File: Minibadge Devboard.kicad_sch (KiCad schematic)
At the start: 37 parts, among them SW1 Power, U1 DRV8837C, U2 74HC4060

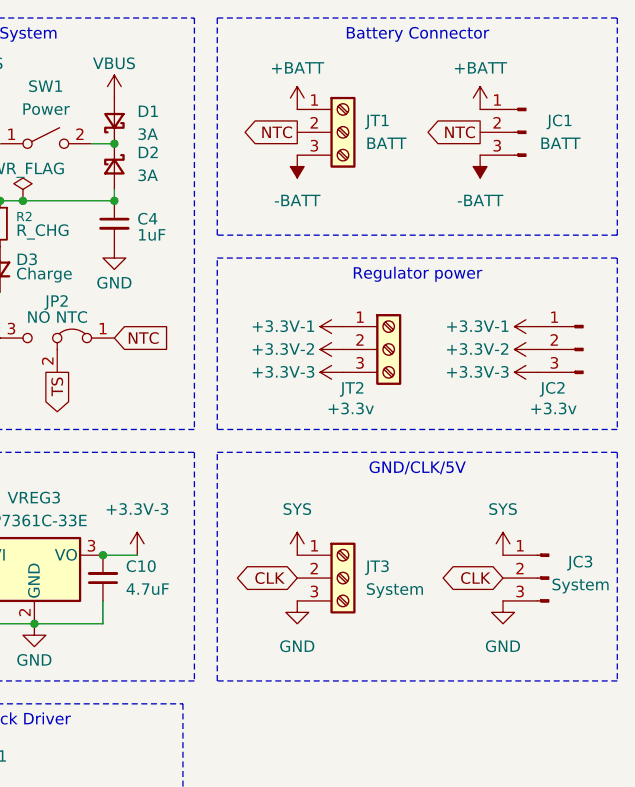
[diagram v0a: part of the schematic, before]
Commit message: Add WAGO 2059 for smaller footprint
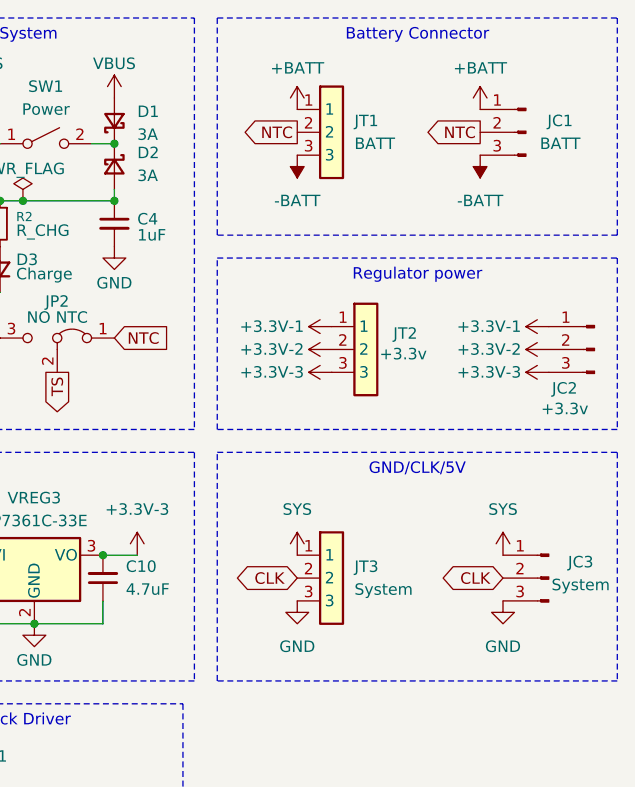
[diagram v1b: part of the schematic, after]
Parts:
- JT1, JT2, JT3: symbol Connector:Screw_Terminal_01x03 -> WAGO 2060:WAGO 2060-3pin; Arrow Part Number (none) -> 2060-453/998-404; Arrow Price/Stock (none) -> https://www.arrow.com/en/products/2060-453998-404/wago-kont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; Height (none) -> 4.5; Manufacturer_Name (none) -> Wago; Manufacturer_Part_Number (none) -> 2060-453/998-404
- U2: footprint 74LV4060D,118:74LV4060D118 -> (none)
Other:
- moved on the sheet: JC2

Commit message: update footprints
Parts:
- JC1, JC2, JC3: footprint Connector_PinSocket_2.54mm:PinSocket_1x03_P2.54mm_Vertical -> Castellated pins:Castellated pins 1x03
- JT1, JT2, JT3: footprint WAGO connectors:WAGO 2060-453 -> WAGO 2059-303:2059-303
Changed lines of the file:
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@@
 			)
 		)
-		(property "Footprint" "WAGO connectors:WAGO 2060-453"
+		(property "Footprint" "WAGO 2059-303:2059-303"
 			(at 200.66 144.45 0)
 			(effects
@@
 			)
 		)
-		(property "Footprint" "Connector_PinSocket_2.54mm:PinSocket_1x03_P2.54mm_Vertical"
+		(property "Footprint" "Castellated pins:Castellated pins 1x03"
 			(at 207.01 52.07 0)
 			(effects
@@
 			)
 		)
-		(property "Footprint" "WAGO connectors:WAGO 2060-453"
+		(property "Footprint" "WAGO 2059-303:2059-303"
 			(at 204.47 168.58 0)
 			(effects
@@
 			)
 		)
-		(property "Footprint" "WAGO connectors:WAGO 2060-453"
+		(property "Footprint" "WAGO 2059-303:2059-303"
 			(at 200.66 193.98 0)
 			(effects
@@
 			)
 		)
-		(property "Footprint" "Connector_PinSocket_2.54mm:PinSocket_1x03_P2.54mm_Vertical"
+		(property "Footprint" "Castellated pins:Castellated pins 1x03"
 			(at 209.55 101.6 0)
 			(effects
@@
 			)
 		)
-		(property "Footprint" "Connector_PinSocket_2.54mm:PinSocket_1x03_P2.54mm_Vertical"
+		(property "Footprint" "Castellated pins:Castellated pins 1x03"
 			(at 214.63 76.2 0)
 			(effects

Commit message: R1
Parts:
- removed JP1: Speed, symbol Jumper:Jumper_3_Bridged12
- removed JP2: NO NTC, symbol Jumper:Jumper_3_Bridged12
- added Q1: PMOS, Package_TO_SOT_SMD:SOT-23, symbol Simulation_SPICE:PMOS
- added R8: 100k, Resistor_SMD:R_0603_1608Metric, symbol Device:R_Small
- added SW3: SPEED, Jumper:SolderJumper-3_P1.3mm_Open_RoundedPad1.0x1.5mm_NumberLabels, symbol Switch:SW_SPDT
- added SW4: NTC, Jumper:SolderJumper-3_P1.3mm_Open_RoundedPad1.0x1.5mm_NumberLabels, symbol Switch:SW_SPDT
- JC1, JC2, JC3: now left out of the parts list
- JT1, JT2, JT3: LCSC Part # (none) -> C3309252
- NT1: footprint (none) -> NetTie:NetTie-2_SMD_Pad2.0mm
- SW1: footprint (none) -> SK12D07VG3-T:SW-SMD_SK12D07VG3-T; LCSC Part # (none) -> C25168821
- U1: LCSC Part # (none) -> C191000
- U2: footprint (none) -> Package_SO:TSSOP-16-1EP_4.4x5mm_P0.65mm; LCSC Part # (none) -> C354054
- USB1: footprint (none) -> Connector_USB:USB_C_Receptacle_HRO_TYPE-C-31-M-17
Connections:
- net +BATT: now also JC1.3 (Pin_3), JT1.3; no longer JC1.1 (Pin_1), JT1.1
- net -BATT: now also JC1.1 (Pin_1), JT1.1; no longer JC1.3 (Pin_3), JT1.3
- net CLK_LOW: now also SW3.2 (B)
- net FAST: now also SW3.1 (A)
- net GND: now also R8.2
- net NTC: now also SW4.3 (C)
- net SLOW: now also SW3.3 (C)
- net SYS: now also Q1.1 (D); no longer SW1.1 (A)
- net TS: now also SW4.2 (B)
- net VDD: now reaches D1.1 (K), D2.1 (K)
- net VDD: now also Q1.3 (S); no longer SW1.2 (B)
- net at R7.1: now also SW4.1 (A)
- new net: Q1.2 (G), SW1.1 (A)
- new net: R8.1, SW1.2 (B)
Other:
- moved on the sheet: BMS1, C1, C10, C2, C3, C4, C5, C6, C7, C8, C9, D1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

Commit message: Add support for external PSU and Power switch
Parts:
- added J1: External power, Castellated pins:Castellated pins 1x02, symbol Connector:Conn_01x02_Pin
- added J2: External switch, Castellated pins:Castellated pins 1x02, symbol Connector:Conn_01x02_Pin
- D3: value Charge -> RED
- R1: value 8.45k -> 8.45kΩ
- R3: value 20k -> 20kΩ
- R4, R5: value 5.1k -> 5.1kΩ
- R6: value 675 -> 675Ω
- R7: value 10k -> 10kΩ
- R8: value 100k -> 100kΩ
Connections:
- net GND: now also J1.1 (Pin_1)
- net VBUS: now also J1.2 (Pin_2)
- net SW1: now reaches Q1.2 (G), SW1.1 (A)
- net SW1: now also J2.1 (Pin_1)
- net SW2: now reaches R8.1, SW1.2 (B)
- net SW2: now also J2.2 (Pin_2)
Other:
- moved on the sheet: BMS1, C1, C10, C2, C3, C4, C5, C6, C7, C8, C9, D1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

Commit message: BOM updates
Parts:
- D1, D2: LCSC Part # (none) -> C382787
- D3: footprint LED_SMD:LED_1206_3216Metric -> LED_SMD:LED_0603_1608Metric; LCSC Part # (none) -> C2286
- J1, J2: now not fitted; now left out of the parts list
- JC1, JC2, JC3: now not fitted
- Q1: LCSC Part # (none) -> C347478
- USB1: LCSC Part # C3743528 -> C283540
- VREG1, VREG2, VREG3: LCSC Part # C3743528 -> C3743528
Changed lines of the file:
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@@
 		(unit 1)
 		(exclude_from_sim no)
-		(in_bom yes)
+		(in_bom no)
 		(on_board yes)
-		(dnp no)
+		(dnp yes)
 		(property "Reference" "J2"
 			(at 146.05 148.082 90)
@@
 			)
 		)
-		(property "Footprint" "LED_SMD:LED_1206_3216Metric"
+		(property "Footprint" "LED_SMD:LED_0603_1608Metric"
 			(at 134.62 52.07 90)
 			(effects
@@
 			)
 		)
+		(property "LCSC Part #" "C2286"
+			(at 134.62 52.07 90)
+			(effects
+				(font
+					(size 1.27 1.27)
+				)
+				(hide yes)
+			)
+		)
 		(pin "2"
 		)
@@
 			)
 		)
-		(property "LCSC Part #" "C3743528 "
+		(property "LCSC Part #" "C3743528"
 			(at 74.93 82.55 0)
 			(effects
@@
 		(in_bom no)
 		(on_board yes)
-		(dnp no)
+		(dnp yes)
 		(property "Reference" "JC1"
 			(at 196.85 36.83 0)
@@
 		(unit 1)
 		(exclude_from_sim no)
-		(in_bom yes)
+		(in_bom no)
 		(on_board yes)
-		(dnp no)
+		(dnp yes)
 		(property "Reference" "J1"
 			(at 129.286 148.082 90)
@@
 			)
 		)
+		(property "LCSC Part #" "C382787"
+			(at 147.32 40.64 90)
+			(effects
+				(font
+					(size 1.27 1.27)
+				)
+				(hide yes)
+			)
+		)
 		(pin "2"
 		)
@@
 			)
 		)
+		(property "LCSC Part #" "C347478"
+			(at 171.45 111.76 0)
+			(effects
+				(font
+					(size 1.27 1.27)
+				)
+				(hide yes)
+			)
+		)
 		(pin "2"
 		)
@@
 			)
 		)
-		(property "LCSC Part #" "C3743528 "
+		(property "LCSC Part #" "C3743528"
 			(at 138.43 82.55 0)
 			(effects
@@
 		(in_bom no)
 		(on_board yes)
-		(dnp no)
+		(dnp yes)
 		(property "Reference" "JC3"
 			(at 199.136 83.312 0)
@@
 			)
 		)
-		(property "LCSC Part #" "C3743528 "
+		(property "LCSC Part #" "C3743528"
 			(at 106.68 82.55 0)
 			(effects
@@
 			)
 		)
-		(property "LCSC Part #" "C3743528 "
+		(property "LCSC Part #" "C283540"
 			(at 71.12 43.18 0)
 			(effects
@@
 			)
 		)
+		(property "LCSC Part #" "C382787"
+			(at 147.32 35.56 90)
+			(effects
+				(font
+					(size 1.27 1.27)
+				)
+				(hide yes)
+			)
+		)
 		(pin "2"
 		)
@@
 		(in_bom no)
 		(on_board yes)
-		(dnp no)
+		(dnp yes)
 		(property "Reference" "JC2"
 			(at 197.358 64.008 0)

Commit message: LCSC part numbers
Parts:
- C1, C2: LCSC Part # (none) -> C14663
- C10, C5, C6, C7, C8, C9: LCSC Part # (none) -> C1779
- C3, C4: LCSC Part # (none) -> C15849
- R1: LCSC Part # (none) -> C25981
- R2: value R_CHG -> R_CHG 120-150Ω
- R3: LCSC Part # (none) -> C4184
- R4, R5: LCSC Part # (none) -> C23186
- R6: LCSC Part # (none) -> C23228
- R7: LCSC Part # (none) -> C25804
- R8: LCSC Part # (none) -> C25803
- SW3, SW4: now left out of the parts list
- VREG1, VREG2, VREG3: LCSC Part # C3743528 -> C500795
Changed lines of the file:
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@@
 			)
 		)
-		(property "LCSC Part #" "C3743528"
+		(property "LCSC Part #" "C500795"
 			(at 74.93 82.55 0)
 			(effects
@@
 			)
 		)
+		(property "LCSC Part #" "C1779"
+			(at 114.3 85.09 0)
+			(effects
+				(font
+					(size 1.27 1.27)
+				)
+				(hide yes)
+			)
+		)
 		(pin "2"
 		)
@@
 			)
 		)
+		(property "LCSC Part #" "C14663"
+			(at 64.77 111.76 90)
+			(effects
+				(font
+					(size 1.27 1.27)
+				)
+				(hide yes)
+			)
+		)
 		(pin "1"
 		)
@@
 			)
 		)
-		(property "Value" "R_CHG"
+		(property "Value" "R_CHG 120-150Ω"
 			(at 136.398 47.752 0)
 			(effects
@@
 			)
 		)
+		(property "LCSC Part #" ""
+			(at 134.62 46.99 0)
+			(effects
+				(font
+					(size 1.27 1.27)
+				)
+				(hide yes)
+			)
+		)
 		(pin "2"
 		)
@@
 			)
 		)
+		(property "LCSC Part #" "C23228"
+			(at 107.95 57.15 0)
+			(effects
+				(font
+					(size 1.27 1.27)
+				)
+				(hide yes)
+			)
+		)
 		(pin "2"
 		)
@@
 			)
 		)
-		(property "LCSC Part #" "C3743528"
+		(property "LCSC Part #" "C500795"
 			(at 138.43 82.55 0)
 			(effects
@@
 			)
 		)
+		(property "LCSC Part #" "C14663"
+			(at 88.9 109.22 90)
+			(effects
+				(font
+					(size 1.27 1.27)
+				)
+				(hide yes)
+			)
+		)
 		(pin "1"
 		)
@@
 		(unit 1)
 		(exclude_from_sim no)
-		(in_bom yes)
+		(in_bom no)
 		(on_board yes)
 		(dnp no)
@@
 			)
 		)
+		(property "LCSC Part #" "C25804"
+			(at 173.99 147.32 90)
+			(effects
+				(font
+					(size 1.27 1.27)
+				)
+				(hide yes)
+			)
+		)
 		(pin "2"
 		)
@@
 		(unit 1)
 		(exclude_from_sim no)
-		(in_bom yes)
+		(in_bom no)
 		(on_board yes)
 		(dnp no)
@@
 			)
 		)
+		(property "LCSC Part #" "C1779"
+			(at 146.05 85.09 0)
+			(effects
+				(font
+					(size 1.27 1.27)
+				)
+				(hide yes)
+			)
+		)
 		(pin "2"
 		)
@@
 			)
 		)
+		(property "LCSC Part #" "C25803"
+			(at 194.31 111.76 90)
+			(effects
+				(font
+					(size 1.27 1.27)
+				)
+				(hide yes)
+			)
+		)
 		(pin "1"
 		)
@@
 			)
 		)
+		(property "LCSC Part #" "C1779"
+			(at 130.81 85.09 0)
+			(effects
+				(font
+					(size 1.27 1.27)
+				)
+				(hide yes)
+			)
+		)
 		(pin "2"
 		)
@@
 			)
 		)
+		(property "LCSC Part #" "C23186"
+			(at 90.17 50.8 90)
+			(effects
+				(font
+					(size 1.27 1.27)
+				)
+				(hide yes)
+			)
+		)
 		(pin "1"
 		)
@@
 			)
 		)
+		(property "LCSC Part #" "C4184"
+			(at 64.77 121.92 90)
+			(effects
+				(font
+					(size 1.27 1.27)
+				)
+				(hide yes)
+			)
+		)
 		(pin "2"
 		)
@@
 			)
 		)
+		(property "LCSC Part #" "C23186"
+			(at 90.17 48.26 90)
+			(effects
+				(font
+					(size 1.27 1.27)
+				)
+				(hide yes)
+			)
+		)
 		(pin "1"
 		)
@@
 			)
 		)
+		(property "LCSC Part #" "C1779"
+			(at 99.06 85.09 0)
+			(effects
+				(font
+					(size 1.27 1.27)
+				)
+				(hide yes)
+			)
+		)
 		(pin "2"
 		)
@@
 			)
 		)
+		(property "LCSC Part #" "C1779"
+			(at 82.55 85.09 0)
+			(effects
+				(font
+					(size 1.27 1.27)
+				)
+				(hide yes)
+			)
+		)
 		(pin "2"
 		)
@@
 			)
 		)
-		(property "LCSC Part #" "C3743528"
+		(property "LCSC Part #" "C500795"
 			(at 106.68 82.55 0)
 			(effects
@@
 			)
 		)
+		(property "LCSC Part #" "C25981"
+			(at 64.77 116.84 90)
+			(effects
+				(font
+					(size 1.27 1.27)
+				)
+				(hide yes)
+			)
+		)
 		(pin "2"
 		)
@@
 			)
 		)
+		(property "LCSC Part #" "C15849"
+			(at 147.32 46.99 0)
+			(effects
+				(font
+					(size 1.27 1.27)
+				)
+				(hide yes)
+			)
+		)
 		(pin "2"
 		)
@@
 			)
 		)
+		(property "LCSC Part #" "C1779"
+			(at 67.31 85.09 0)
+			(effects
+				(font
+					(size 1.27 1.27)
+				)
+				(hide yes)
+			)
+		)
 		(pin "2"
 		)
@@
 			(at 104.14 46.99 0)
 			(effects
+				(font
+					(size 1.27 1.27)
+				)
+				(hide yes)
+			)
+		)
+		(property "LCSC Part #" "C15849"
+			(at 104.14 46.99 0)
+			(effects

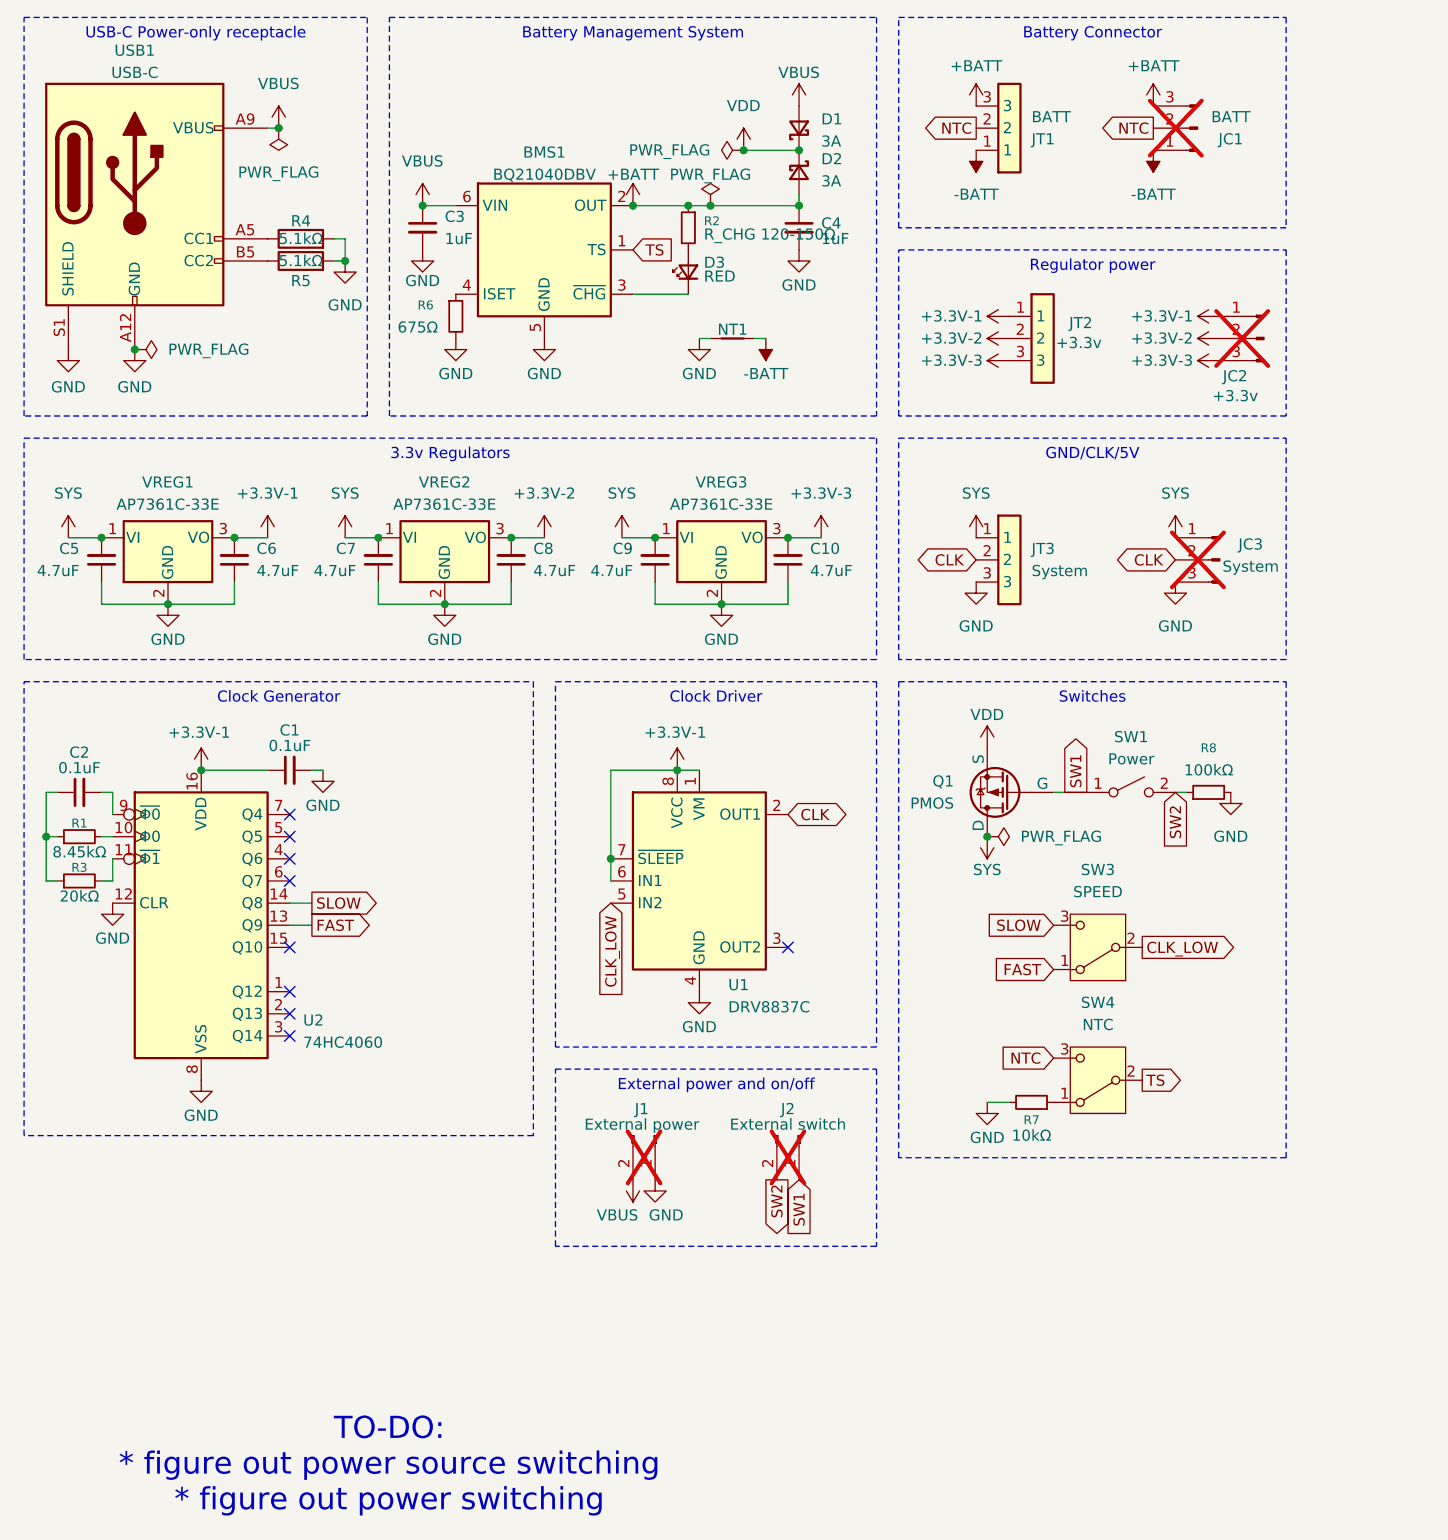
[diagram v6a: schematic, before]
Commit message: Fixes
* Added text to the footprint to clarify which castellated pin is what
* Fixed pinout issue with footprint and symbol. SYS and GND were reversed (yikes)
* Updated schematic symbols and values
* push updated schematic PDF
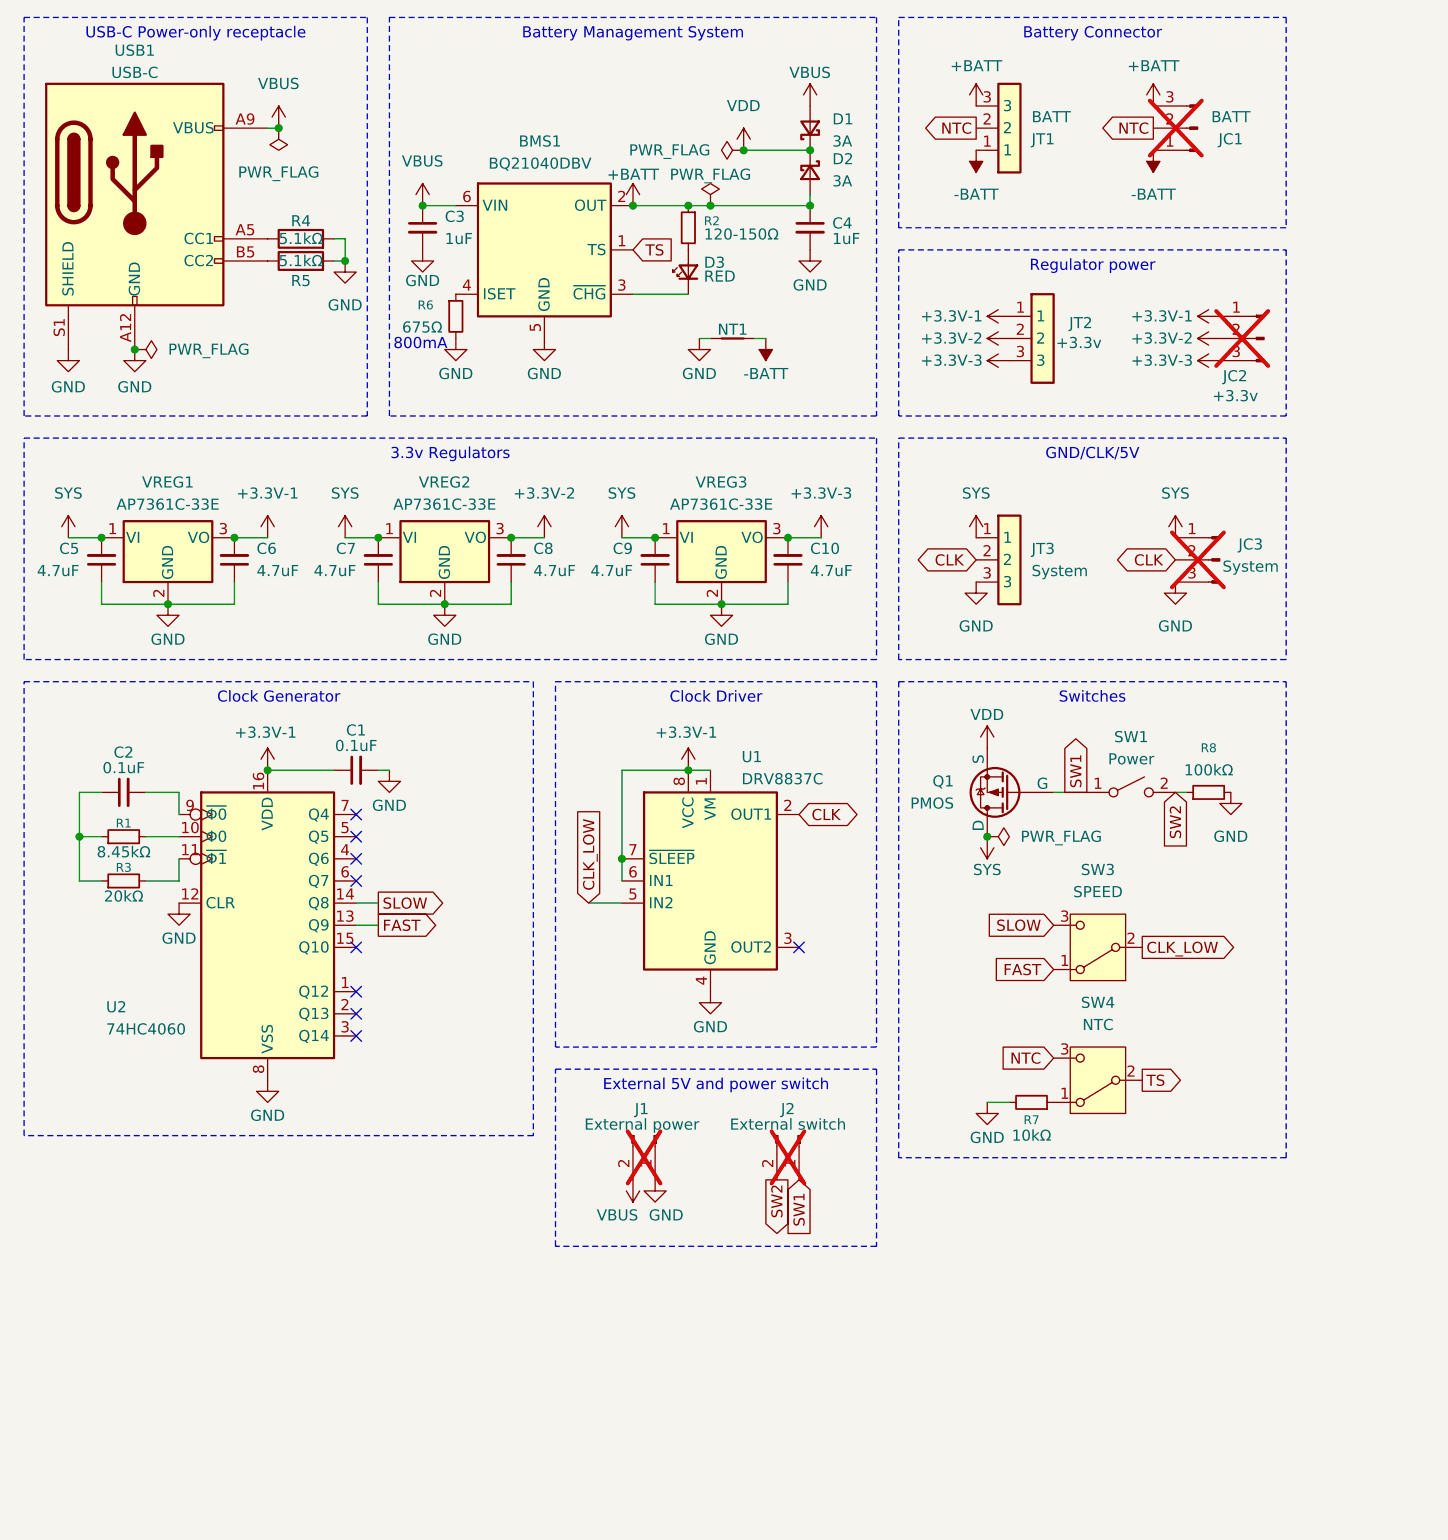
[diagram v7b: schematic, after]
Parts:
- R2: value R_CHG 120-150Ω -> 120-150Ω
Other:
- note added: "800mA"
- note removed: "TO-DO: * figure out power source switching * figure out power switching"
- moved on the sheet: C1, C2, C4, D1, D2, R1, R3, U1, U2
